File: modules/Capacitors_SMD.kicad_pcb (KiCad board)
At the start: 2 copper layers, 9 parts

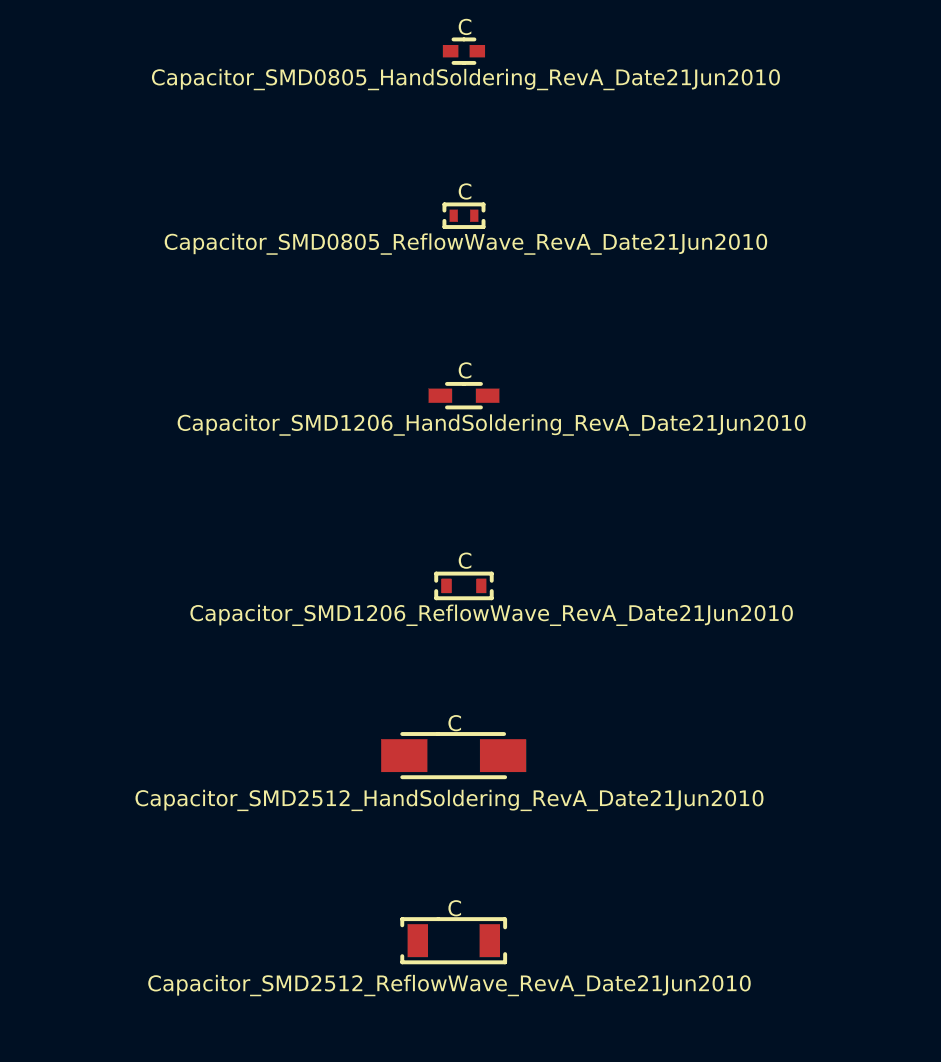
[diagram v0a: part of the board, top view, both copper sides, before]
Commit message: Many librairies renamed. Make sure to use the corresponding fp-lib-table.
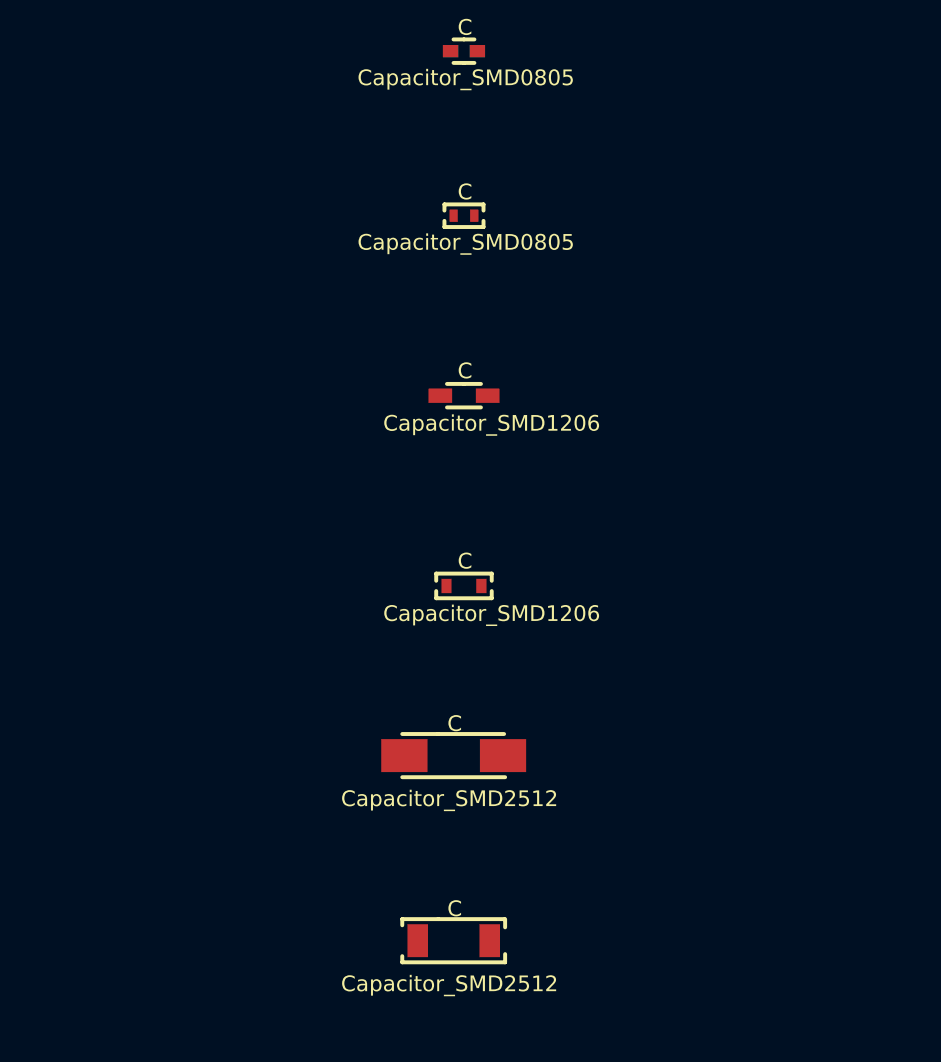
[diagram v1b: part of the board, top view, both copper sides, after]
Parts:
- C: value Capacitor_SMD0805_HandSoldering_RevA_Date21Jun2010 -> Capacitor_SMD0805; footprint Capacitor_SMD0805_HandSoldering_RevA_Date21Jun2010 -> Capacitor_SMD0805
- C: value Capacitor_SMD0805_ReflowWave_RevA_Date21Jun2010 -> Capacitor_SMD0805; footprint Capacitor_SMD0805_ReflowWave_RevA_Date21Jun2010 -> Capacitor_SMD0805
- C: value Capacitor_SMD1206_HandSoldering_RevA_Date21Jun2010 -> Capacitor_SMD1206; footprint Capacitor_SMD1206_HandSoldering_RevA_Date21Jun2010 -> Capacitor_SMD1206
- C: value Capacitor_SMD1206_ReflowWave_RevA_Date21Jun2010 -> Capacitor_SMD1206; footprint Capacitor_SMD1206_ReflowWave_RevA_Date21Jun2010 -> Capacitor_SMD1206
- C: value Capacitor_SMD2512_HandSoldering_RevA_Date21Jun2010 -> Capacitor_SMD2512; footprint Capacitor_SMD2512_HandSoldering_RevA_Date21Jun2010 -> Capacitor_SMD2512
- C: value Capacitor_SMD2512_ReflowWave_RevA_Date21Jun2010 -> Capacitor_SMD2512; footprint Capacitor_SMD2512_ReflowWave_RevA_Date21Jun2010 -> Capacitor_SMD2512
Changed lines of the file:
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@@
     (fp_circle (center 0 0) (end 5.588 0) (layer F.SilkS) (width 0.381))
   )
-  (module Capacitor_SMD0805_HandSoldering_RevA_Date21Jun2010 (layer Vorderseite)
+  (module Capacitor_SMD0805 (layer Vorderseite)
     (at 184 42.5)
     (descr "Capacitor, SMD, 0805, Hand soldering,")
@@
       (effects (font (size 1.524 1.524) (thickness 0.3048)))
     )
-    (fp_text value Capacitor_SMD0805_HandSoldering_RevA_Date21Jun2010 (at 0.20066 2.60096) (layer F.SilkS)
+    (fp_text value Capacitor_SMD0805 (at 0.20066 2.60096) (layer F.SilkS)
       (effects (font (size 1.524 1.524) (thickness 0.3048)))
     )
@@
     )
   )
-  (module Capacitor_SMD0805_ReflowWave_RevA_Date21Jun2010 (layer Vorderseite)
+  (module Capacitor_SMD0805 (layer Vorderseite)
     (at 184 58.5)
     (descr "Capacitor, SMD, 0805, Reflow, Wave,")
@@
       (effects (font (size 1.524 1.524) (thickness 0.3048)))
     )
-    (fp_text value Capacitor_SMD0805_ReflowWave_RevA_Date21Jun2010 (at 0.20066 2.60096) (layer F.SilkS)
+    (fp_text value Capacitor_SMD0805 (at 0.20066 2.60096) (layer F.SilkS)
       (effects (font (size 1.524 1.524) (thickness 0.3048)))
     )
@@
     )
   )
-  (module Capacitor_SMD1206_HandSoldering_RevA_Date21Jun2010 (layer Vorderseite)
+  (module Capacitor_SMD1206 (layer Vorderseite)
     (at 184 76)
     (descr "Capacitor, SMD, 1206, HandSoldering,")
@@
       (effects (font (size 1.524 1.524) (thickness 0.3048)))
     )
-    (fp_text value Capacitor_SMD1206_HandSoldering_RevA_Date21Jun2010 (at 2.70002 2.70002) (layer F.SilkS)
+    (fp_text value Capacitor_SMD1206 (at 2.70002 2.70002) (layer F.SilkS)
       (effects (font (size 1.524 1.524) (thickness 0.3048)))
     )
@@
     )
   )
-  (module Capacitor_SMD1206_ReflowWave_RevA_Date21Jun2010 (layer Vorderseite)
+  (module Capacitor_SMD1206 (layer Vorderseite)
     (at 184 94.5)
     (descr "Capacitor, SMD, 1206, Reflow, Wave,")
@@
       (effects (font (size 1.524 1.524) (thickness 0.3048)))
     )
-    (fp_text value Capacitor_SMD1206_ReflowWave_RevA_Date21Jun2010 (at 2.70002 2.70002) (layer F.SilkS)
+    (fp_text value Capacitor_SMD1206 (at 2.70002 2.70002) (layer F.SilkS)
       (effects (font (size 1.524 1.524) (thickness 0.3048)))
     )
@@
     )
   )
-  (module Capacitor_SMD2512_HandSoldering_RevA_Date21Jun2010 (layer Vorderseite)
+  (module Capacitor_SMD2512 (layer Vorderseite)
     (at 183 111)
     (descr "Capacitor, SMD, 2512, Hand soldering,")
@@
       (effects (font (size 1.524 1.524) (thickness 0.3048)))
     )
-    (fp_text value Capacitor_SMD2512_HandSoldering_RevA_Date21Jun2010 (at -0.39878 4.20116) (layer F.SilkS)
+    (fp_text value Capacitor_SMD2512 (at -0.39878 4.20116) (layer F.SilkS)
       (effects (font (size 1.524 1.524) (thickness 0.3048)))
     )
@@
     )
   )
-  (module Capacitor_SMD2512_ReflowWave_RevA_Date21Jun2010 (layer Vorderseite)
+  (module Capacitor_SMD2512 (layer Vorderseite)
     (at 183 129)
     (descr "Capacitor, SMD, 2512, Reflow, Wave,")
@@
       (effects (font (size 1.524 1.524) (thickness 0.3048)))
     )
-    (fp_text value Capacitor_SMD2512_ReflowWave_RevA_Date21Jun2010 (at -0.39878 4.20116) (layer F.SilkS)
+    (fp_text value Capacitor_SMD2512 (at -0.39878 4.20116) (layer F.SilkS)
       (effects (font (size 1.524 1.524) (thickness 0.3048)))
     )
